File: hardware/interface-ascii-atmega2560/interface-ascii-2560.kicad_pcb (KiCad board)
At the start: 2 copper layers, 88.9 x 132.1 mm, 49 parts, among them J1 Apple 2, J10 Keyboard, J2 Apple 1, J3 UART, J4 Conn_01x05, J5 SOL-20, J6 Conn_01x10, J7 Custom Connector, J8 Custom Connector, SW1 Options, U1 ATmega2560-16AU, Y1 16.000 MHz

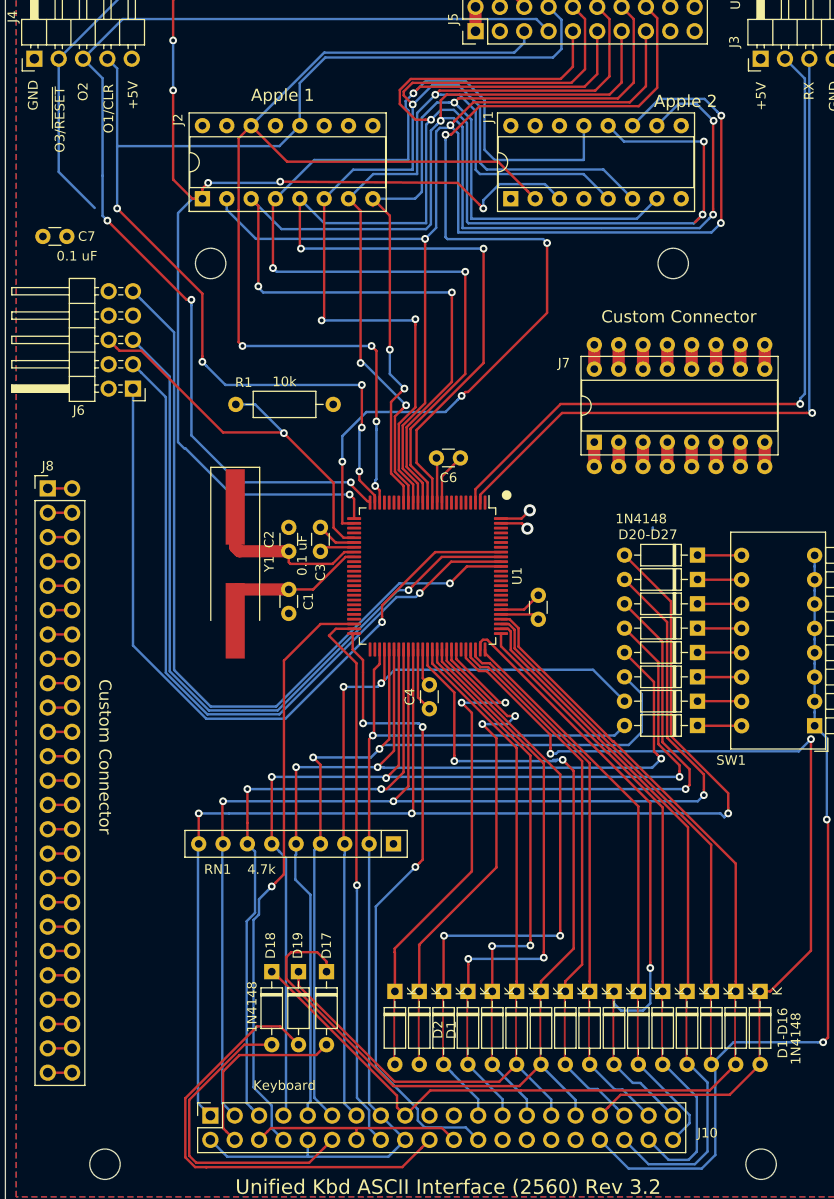
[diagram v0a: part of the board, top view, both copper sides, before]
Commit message: Add additional mounting holes to ASCII interface PCBS and Sol-20 PCB
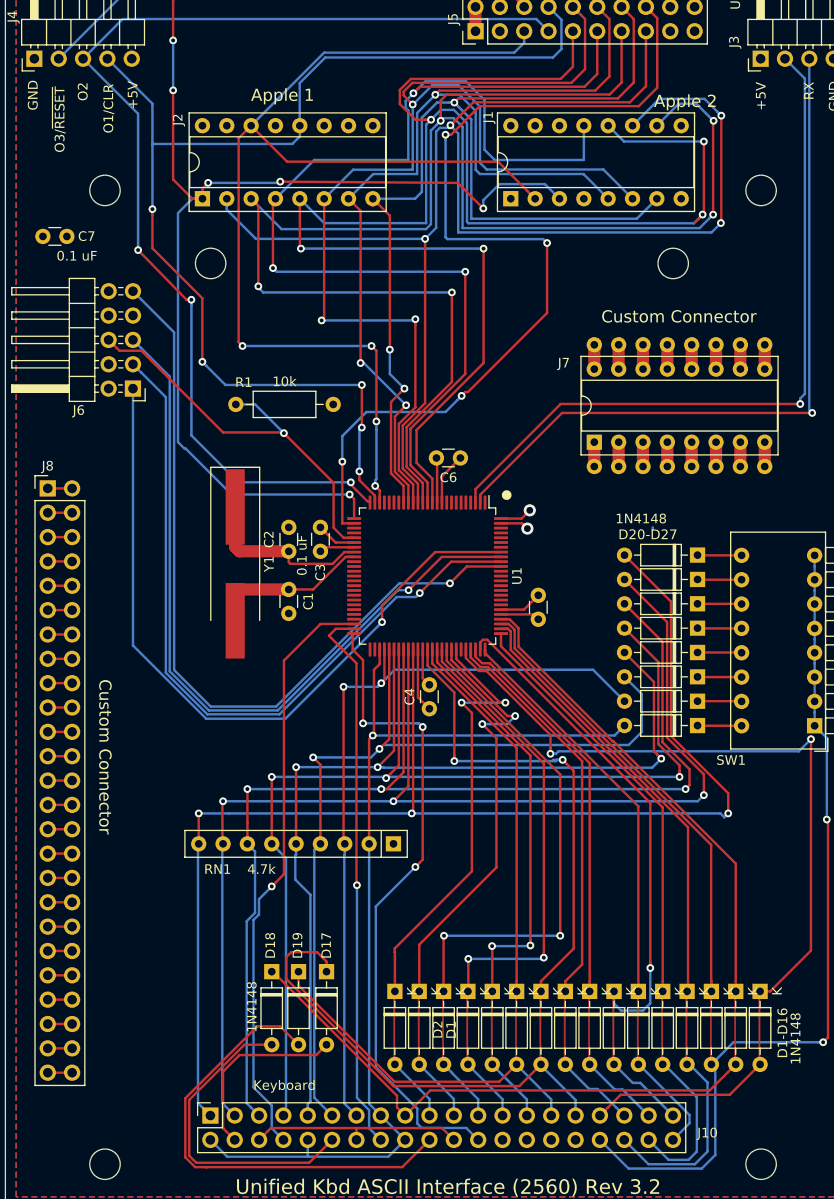
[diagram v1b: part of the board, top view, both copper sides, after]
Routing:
- net /OUT3: track 184.6 -> 167.5 mm
- net /Row5: track 0.00 -> 6.83 mm
- net /Row6: track 0.00 -> 6.83 mm
- net /OUT1: track 124.5 -> 121.5 mm
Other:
- outline, holes or cut-outs redrawn
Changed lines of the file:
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@@
   (general
     (thickness 1.6)
-    (drawings 34)
-    (tracks 993)
+    (drawings 36)
+    (tracks 998)
     (zones 0)
     (modules 49)
@@
     )
   )
+  (gr_circle (center 174.2224 76.5048) (end 175.8099 76.5048) (layer Edge.Cuts) (width 0.1))
+  (gr_circle (center 242.6754 76.5048) (end 244.2629 76.5048) (layer Edge.Cuts) (width 0.1))
   (gr_text D20-D27 (at 230.863 112.422) (layer F.SilkS)
     (effects (font (size 1.016 1.016) (thickness 0.127)))
@@
   (segment (start 213.1592 171.3246) (end 213.1592 173.0264) (width 0.254) (layer B.Cu) (net 5))
   (segment (start 210.428599 168.593999) (end 213.1592 171.3246) (width 0.254) (layer B.Cu) (net 5))
+  (segment (start 210.6192 171.3016) (end 210.6192 173.0264) (width 0.254) (layer B.Cu) (net 6))
+  (segment (start 207.01 167.6924) (end 210.6192 171.3016) (width 0.254) (layer B.Cu) (net 6))
   (segment (start 239.230001 168.492399) (end 240.03 167.6924) (width 0.254) (layer F.Cu) (net 7))
   (segment (start 237.315389 170.407011) (end 239.230001 168.492399) (width 0.254) (layer F.Cu) (net 7))
@@
   (via (at 184 141.505) (size 0.8128) (drill 0.4064) (layers F.Cu B.Cu) (net 22))
   (segment (start 184 144.68) (end 184 141.505) (width 0.254) (layer F.Cu) (net 22))
+  (segment (start 208.0792 171.3016) (end 208.0792 173.0264) (width 0.254) (layer B.Cu) (net 23))
+  (segment (start 204.47 167.6924) (end 208.0792 171.3016) (width 0.254) (layer B.Cu) (net 23))
   (segment (start 218.2392 171.35) (end 218.2392 173.0264) (width 0.254) (layer B.Cu) (net 24))
   (segment (start 214.6578 167.7686) (end 218.2392 171.35) (width 0.254) (layer B.Cu) (net 24))
@@
   (via (at 201.018 96.801) (size 0.8128) (drill 0.4064) (layers F.Cu B.Cu) (net 56))
   (segment (start 201.018 100.219986) (end 201.018 96.801) (width 0.254) (layer F.Cu) (net 56))
-  (segment (start 175.5164 71.8836) (end 192.416566 71.8836) (width 0.254) (layer B.Cu) (net 56))
-  (segment (start 192.416566 71.8836) (end 194.550166 69.75) (width 0.254) (layer B.Cu) (net 56))
-  (via (at 175.491 78.386) (size 0.8128) (drill 0.4064) (layers F.Cu B.Cu) (net 56))
-  (segment (start 175.491 71.909) (end 175.491 78.386) (width 0.254) (layer B.Cu) (net 56))
-  (segment (start 175.491 63.781) (end 175.491 71.909) (width 0.254) (layer B.Cu) (net 56))
-  (segment (start 174.475 62.765) (end 175.491 63.781) (width 0.254) (layer B.Cu) (net 56))
   (via (at 184.381 94.388) (size 0.8128) (drill 0.4064) (layers F.Cu B.Cu) (net 56))
   (segment (start 201.018 96.801) (end 186.794 96.801) (width 0.254) (layer B.Cu) (net 56))
   (segment (start 184.787399 94.794399) (end 184.381 94.388) (width 0.254) (layer B.Cu) (net 56))
   (segment (start 186.794 96.801) (end 184.787399 94.794399) (width 0.254) (layer B.Cu) (net 56))
-  (segment (start 184.381 87.276) (end 184.381 93.813264) (width 0.254) (layer F.Cu) (net 56))
-  (segment (start 175.491 78.386) (end 184.381 87.276) (width 0.254) (layer F.Cu) (net 56))
-  (segment (start 184.381 93.813264) (end 184.381 94.388) (width 0.254) (layer F.Cu) (net 56))
   (segment (start 221.846 58.701) (end 220.4998 57.3548) (width 0.254) (layer B.Cu) (net 56))
   (segment (start 221.846 61.749) (end 221.846 58.701) (width 0.254) (layer B.Cu) (net 56))
@@
   (segment (start 194.541 69.740834) (end 194.541 65.305) (width 0.254) (layer B.Cu) (net 56))
   (segment (start 194.550166 69.75) (end 194.541 69.740834) (width 0.254) (layer B.Cu) (net 56))
+  (via (at 179.173998 78.4622) (size 0.8128) (drill 0.4064) (layers F.Cu B.Cu) (net 56))
+  (segment (start 179.173998 67.463998) (end 174.475 62.765) (width 0.254) (layer B.Cu) (net 56))
+  (segment (start 194.550166 70.88137) (end 193.776536 71.655) (width 0.254) (layer B.Cu) (net 56))
+  (segment (start 194.550166 69.75) (end 194.550166 70.88137) (width 0.254) (layer B.Cu) (net 56))
+  (segment (start 193.776536 71.655) (end 179.2502 71.655) (width 0.254) (layer B.Cu) (net 56))
+  (segment (start 179.2502 71.655) (end 179.173998 71.731202) (width 0.254) (layer B.Cu) (net 56))
+  (segment (start 179.173998 71.731202) (end 179.173998 67.463998) (width 0.254) (layer B.Cu) (net 56))
+  (segment (start 179.173998 78.4622) (end 179.173998 71.731202) (width 0.254) (layer B.Cu) (net 56))
+  (segment (start 184.381 87.7586) (end 179.173998 82.551598) (width 0.254) (layer F.Cu) (net 56))
+  (segment (start 179.173998 79.036936) (end 179.173998 78.4622) (width 0.254) (layer F.Cu) (net 56))
+  (segment (start 179.173998 82.551598) (end 179.173998 79.036936) (width 0.254) (layer F.Cu) (net 56))
+  (segment (start 184.381 94.388) (end 184.381 87.7586) (width 0.254) (layer F.Cu) (net 56))
   (segment (start 201.726 108.9275) (end 201.5875 108.9275) (width 0.254) (layer F.Cu) (net 57))
   (segment (start 201.876 109.0775) (end 201.726 108.9275) (width 0.254) (layer F.Cu) (net 57))
@@
   (segment (start 176.0752 58.6248) (end 219.2298 58.6248) (width 0.254) (layer B.Cu) (net 57))
   (segment (start 171.935 62.765) (end 176.0752 58.6248) (width 0.254) (layer B.Cu) (net 57))
-  (segment (start 173.967 64.797) (end 171.935 62.765) (width 0.254) (layer B.Cu) (net 57))
-  (segment (start 173.967 74.957) (end 173.967 64.797) (width 0.254) (layer B.Cu) (net 57))
-  (segment (start 173.967 74.957) (end 173.967 79.148) (width 0.254) (layer B.Cu) (net 57))
-  (via (at 174.475 79.656) (size 0.8128) (drill 0.4064) (layers F.Cu B.Cu) (net 57))
-  (segment (start 173.967 79.148) (end 174.475 79.656) (width 0.254) (layer B.Cu) (net 57))
   (segment (start 183.238 88.485736) (end 183.238 87.911) (width 0.254) (layer B.Cu) (net 57))
   (segment (start 188.130751 106.961) (end 183.238 102.068249) (width 0.254) (layer B.Cu) (net 57))
@@
   (segment (start 199.875 106.961) (end 188.130751 106.961) (width 0.254) (layer B.Cu) (net 57))
   (segment (start 183.238 102.068249) (end 183.238 88.485736) (width 0.254) (layer B.Cu) (net 57))
-  (segment (start 174.475 79.656) (end 182.73 87.911) (width 0.254) (layer F.Cu) (net 57))
   (via (at 183.238 87.911) (size 0.8128) (drill 0.4064) (layers F.Cu B.Cu) (net 57))
+  (segment (start 177.5992 82.7802) (end 177.6246 82.7802) (width 0.254) (layer F.Cu) (net 57))
+  (segment (start 177.6754 82.7294) (end 182.73 87.911) (width 0.254) (layer F.Cu) (net 57))
+  (via (at 177.6754 82.7294) (size 0.8128) (drill 0.4064) (layers F.Cu B.Cu) (net 57))
+  (segment (start 177.6246 82.7802) (end 177.6754 82.7294) (width 0.254) (layer F.Cu) (net 57))
+  (segment (start 177.6754 68.5054) (end 171.935 62.765) (width 0.254) (layer B.Cu) (net 57))
+  (segment (start 177.6754 82.7294) (end 177.6754 68.5054) (width 0.254) (layer B.Cu) (net 57))
   (segment (start 184.254 77.497) (end 184.381 77.497) (width 0.254) (layer B.Cu) (net 58))
   (via (at 213.6926 78.386) (size 0.8128) (drill 0.4064) (layers F.Cu B.Cu) (net 58))
@@
   (segment (start 200.2135 108.6965) (end 199.748 108.231) (width 0.254) (layer F.Cu) (net 58))
   (segment (start 200.2135 110.74) (end 200.2135 108.6965) (width 0.254) (layer F.Cu) (net 58))
-  (segment (start 169.395 74.576) (end 169.395 62.765) (width 0.254) (layer B.Cu) (net 58))
-  (segment (start 173.15419 78.33519) (end 169.395 74.576) (width 0.254) (layer B.Cu) (net 58))
   (segment (start 176.036201 56.123799) (end 169.395 62.765) (width 0.254) (layer B.Cu) (net 58))
   (segment (start 181.333 56.123799) (end 176.036201 56.123799) (width 0.254) (layer B.Cu) (net 58))
@@
   (segment (start 207.368 132.488) (end 207.368 146.331) (width 0.254) (layer F.Cu) (net 59))
   (segment (start 207.012399 146.686601) (end 206.606 147.093) (width 0.254) (layer F.Cu) (net 59))
-  (segment (start 211.8638 174.271) (end 213.1592 175.5664) (width 0.254) (layer B.Cu) (net 59))
-  (segment (start 207.581838 174.271) (end 211.8638 174.271) (width 0.254) (layer B.Cu) (net 59))
-  (segment (start 206.86 172.366) (end 206.86 173.549162) (width 0.254) (layer B.Cu) (net 59))
-  (segment (start 202.4785 167.9845) (end 206.86 172.366) (width 0.254) (layer B.Cu) (net 59))
-  (segment (start 206.86 173.549162) (end 207.581838 174.271) (width 0.254) (layer B.Cu) (net 59))
+  (segment (start 207.2664 174.3218) (end 211.9146 174.3218) (width 0.254) (layer B.Cu) (net 59))
+  (segment (start 206.8092 173.8646) (end 207.2664 174.3218) (width 0.254) (layer B.Cu) (net 59))
+  (segment (start 202.4785 167.9845) (end 206.8092 172.3152) (width 0.254) (layer B.Cu) (net 59))
+  (segment (start 206.8092 172.3152) (end 206.8092 173.8646) (width 0.254) (layer B.Cu) (net 59))
+  (segment (start 211.9146 174.3218) (end 213.1592 175.5664) (width 0.254) (layer B.Cu) (net 59))
   (segment (start 202.4785 151.2205) (end 202.4785 167.9845) (width 0.254) (layer B.Cu) (net 59))
   (segment (start 206.606 147.093) (end 202.4785 151.2205) (width 0.254) (layer B.Cu) (net 59))

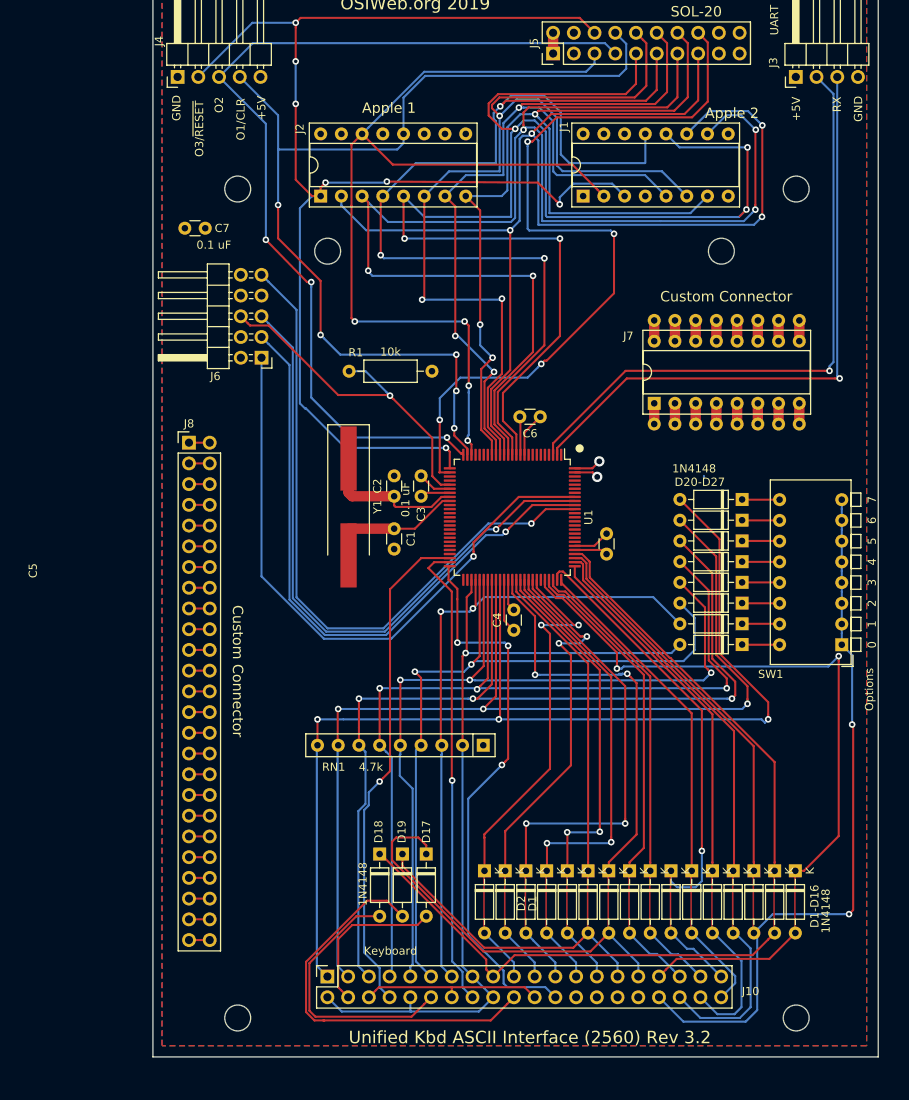
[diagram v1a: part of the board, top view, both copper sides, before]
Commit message: Include both ISP and JTAG ports in programming header
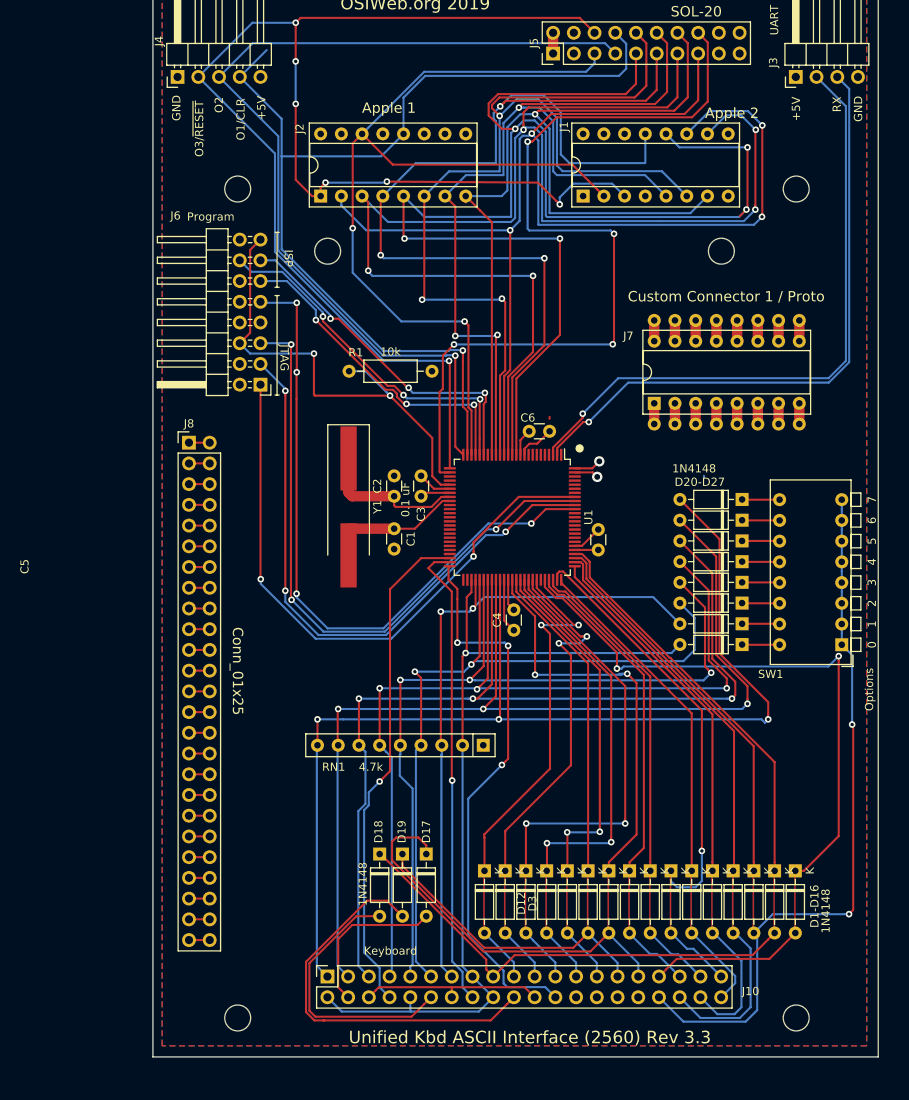
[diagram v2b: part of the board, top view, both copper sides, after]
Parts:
- removed C7: 0.1 uF, Capacitor_THT:C_Disc_D3.0mm_W1.6mm_P2.50mm
- J6: value Conn_01x10 -> Program; footprint Connector_PinHeader_2.54mm:PinHeader_2x05_P2.54mm_Horizontal -> Connector_PinHeader_2.54mm:PinHeader_2x08_P2.54mm_Horizontal
- J7: value Custom Connector -> Custom Connector 1 / Proto
- J8: value Custom Connector -> Conn_01x25
- moved J6 3.30 mm to (177.0, 100.5)
- moved C6 2.11 mm to (212.4, 106.2)
- moved C5 1.14 mm to (218.4, 120.7)
- renumbered D3 to D1, D2 to D12, D12 to D2, D1 to D3
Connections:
- U1 pad 20: Net-(U1-Pad20) -> /SCK
- U1 pad 21: Net-(U1-Pad21) -> /MOSI
- U1 pad 22: Net-(U1-Pad22) -> /MISO
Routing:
- net /MOSI: track 0.00 -> 44.0 mm, vias 0 -> 3
- net /SCK: track 0.00 -> 42.3 mm, vias 0 -> 3
- net /MISO: track 0.00 -> 39.5 mm, vias 0 -> 3
- net /OUT3: track 167.5 -> 184.0 mm
- net /~RESET: track 43.2 -> 58.6 mm, vias 1 -> 2
- net /D7: track 99.0 -> 105.3 mm
- net /~STROBE: track 120.6 -> 116.7 mm, vias 4 -> 2
- net /TDO: track 77.0 -> 74.2 mm, vias 1 -> 3
- net /TCK: track 76.6 -> 74.0 mm, vias 1 -> 2
- net /D5: track 105.6 -> 107.8 mm
- net GND: track 22.4 -> 20.2 mm
- net /OUT2: track 116.8 -> 114.7 mm, vias 3 -> 1
- net VCC: track 46.3 -> 44.6 mm
- net /Tx: track 76.1 -> 77.8 mm
- net /D1: track 130.5 -> 129.0 mm
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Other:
- board text added: "ISP"
- board text added: "JTAG"
- board text added: "Unified Kbd ASCII Interface (2560) Rev 3.3"
- board text removed: "Unified Kbd ASCII Interface (2560) Rev 3.2"

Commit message: Add mounting holes for Apple II keyboard
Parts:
- added MH1: Apple II, MountingHole:MountingHole_3.7mm, F.Cu at (169.5, 101.2)
- added MH2: Apple II, MountingHole:MountingHole_3.7mm, F.Cu at (169.5, 177.4)
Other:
- board text added: "Unified Kbd ASCII Interface (2560) Rev 3.4"
- board text removed: "Unified Kbd ASCII Interface (2560) Rev 3.3"
